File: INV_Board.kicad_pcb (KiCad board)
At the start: 2 copper layers, 100 x 50 mm, 142 parts, among them J1 USB_B_Micro, J10 Conn_01x02_Male, J11 Conn_01x04_Male, J2 Conn_01x02_Male, J3 Conn_01x02_Male, J4 Conn_01x02_Male, J5 Conn_01x04_Male, J6 Conn_01x03_Male, J7 Conn_01x03_Male, J8 Conn_ARM_JTAG_SWD_10, J9 Conn_01x05_Male, Q1 Q_NMOS_GDS, Q2 Q_NMOS_GDS, Q3 Q_NMOS_GDS, Q4 Q_NMOS_GDS, Q5 Q_NMOS_GDS, Q6 Q_NMOS_GDS, U1 LMR36510, U2 STM32F303CBTx, U3 IR2181, U4 IR2181, U5 IR2181, U6 TPS76333, U7 TLV61046ADB, X1 ASE-xxxMHz

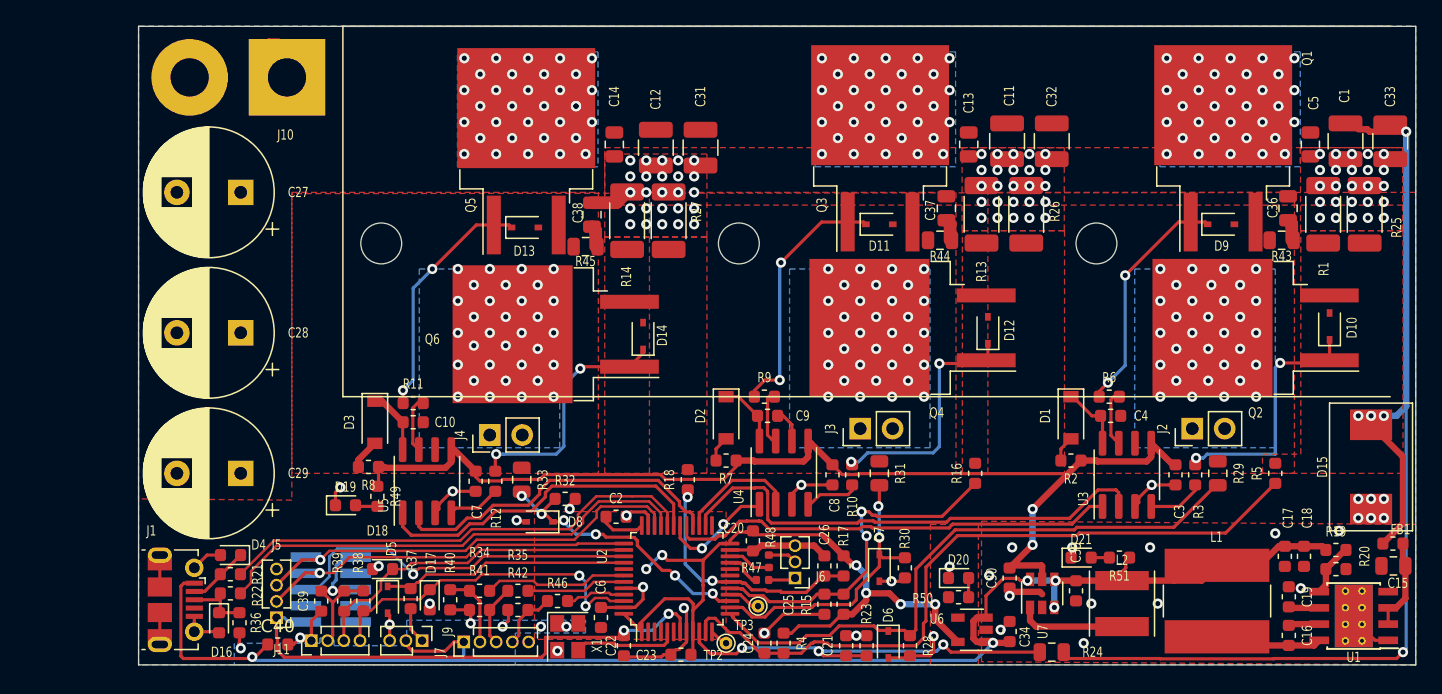
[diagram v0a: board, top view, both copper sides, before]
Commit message: Connectors now JST PH series for throttle and hall sensor input, routing for Iu improved, larger capacitors (2x) 6 pin header to include SWO connectivity, 0402 removed, extra capacitors on Hall sensor lines, extra resistor added to enable use of 100V TI LM5163 chip or LMR36510.
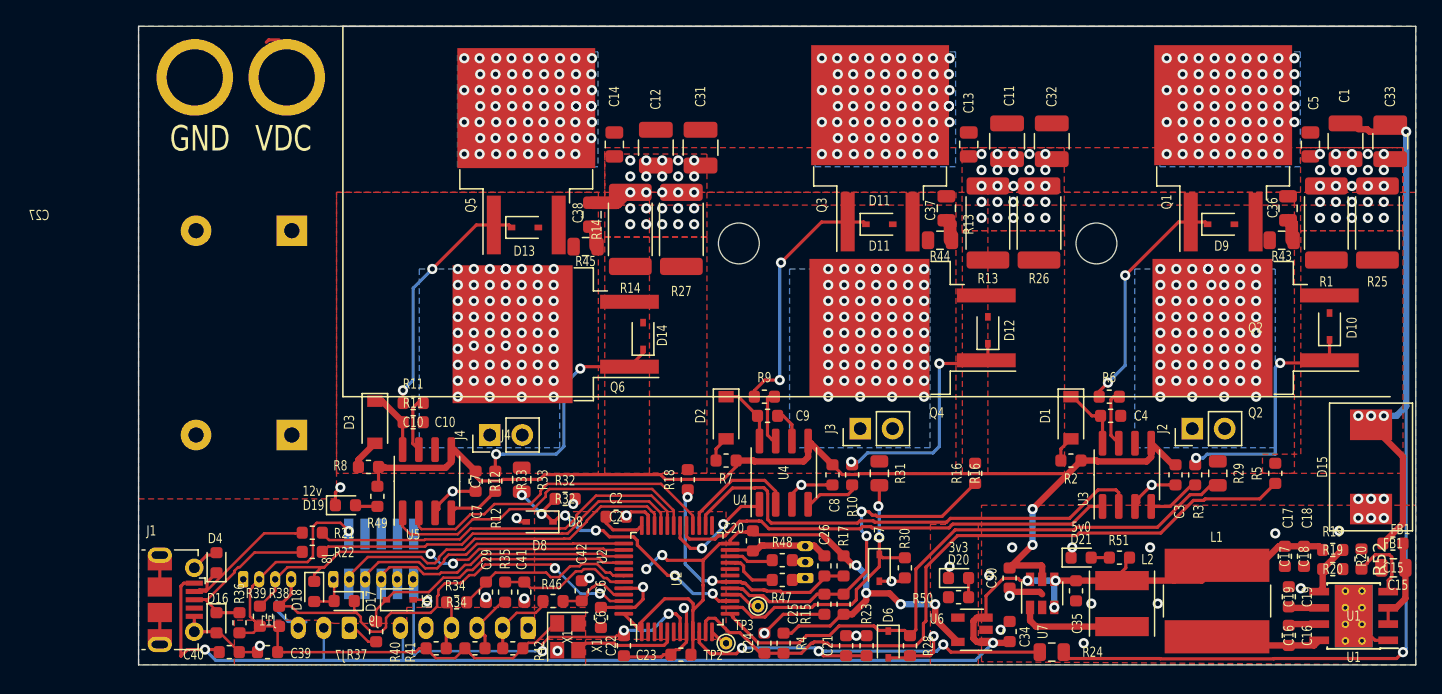
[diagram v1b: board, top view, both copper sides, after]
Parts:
- removed J5: Conn_01x04_Male, Connector_PinHeader_1.27mm:PinHeader_1x04_P1.27mm_Vertical
- added C41: C_100pF_16V, Capacitor_SMD:C_0603_1608Metric, F.Cu at (70.2, 72.3)
- added C42: C_100pF_16V, Capacitor_SMD:C_0603_1608Metric, F.Cu at (74.7, 72.2)
- added J12: Conn_01x06_Female, Connector_JST:JST_PH_B6B-PH-K_1x06_P2.00mm_Vertical, B.Cu at (70.5, 75.1)
- added R52: R_30k, Resistor_SMD:R_0603_1608Metric, F.Cu at (135.8, 69.7)
- C1, C11, C12, C31, C32, C33: value C_10uF 75V -> C_4.7uF 100V
- C21, C24, C25, C26: value C_100pF_25V -> C_100pF_16V
- C27, C28: value CP_220uF -> CP_470uF+; footprint Capacitor_THT:CP_Radial_D10.0mm_P5.00mm -> Capacitor_THT:CP_Radial_D16.0mm_P7.50mm; moved to B.Cu
- C29: value CP_220uF -> C_100pF_16V; footprint Capacitor_THT:CP_Radial_D10.0mm_P5.00mm -> Capacitor_SMD:C_0603_1608Metric
- J10: footprint Connector_Wire:SolderWirePad_1x02_P7.62mm_Drill2.5mm -> INV_Board:XT60; moved to B.Cu
- J11: footprint Connector_PinHeader_1.27mm:PinHeader_1x04_P1.27mm_Vertical -> Connector_Molex:Molex_PicoBlade_53047-0410_1x04_P1.25mm_Vertical; moved to B.Cu
- J6: footprint Connector_PinHeader_1.27mm:PinHeader_1x03_P1.27mm_Vertical -> Connector_Molex:Molex_PicoBlade_53047-0310_1x03_P1.25mm_Vertical; moved to B.Cu
- J7: footprint Connector_PinHeader_1.27mm:PinHeader_1x03_P1.27mm_Vertical -> Connector_JST:JST_PH_B3B-PH-K_1x03_P2.00mm_Vertical; moved to B.Cu
- J9: value Conn_01x05_Male -> Conn_01x06_Male; footprint Connector_PinHeader_1.27mm:PinHeader_1x05_P1.27mm_Vertical -> Connector_Molex:Molex_PicoBlade_53047-0610_1x06_P1.25mm_Vertical; moved to B.Cu
- R1, R13, R14, R25, R26, R27: footprint Resistor_SMD:R_2010_5025Metric -> Resistor_SMD:R_2512_6332Metric
- R47, R48: footprint Resistor_SMD:R_0402_1005Metric -> Resistor_SMD:R_0603_1608Metric
- moved C29 21.3 mm to (67.2, 72.3), turned to 270 degrees
- moved J9 11.3 mm to (55.2, 71.3), turned to 0 degrees
- moved C28 8.94 mm to (52.0, 60.0)
- moved R21 7.19 mm to (53.6, 67.7)
- moved R22 7.19 mm to (53.6, 69.2)
- moved J11 7.17 mm to (48.2, 71.3), turned to 0 degrees
- moved R38 6.71 mm to (51.0, 74.2), turned to 90 degrees
- moved R39 6.71 mm to (49.5, 74.2), turned to 90 degrees
- moved D17 6.70 mm to (56.1, 73.0), turned to 180 degrees
- moved C39 5.80 mm to (50.1, 77.0), turned to 180 degrees
- moved J7 5.79 mm to (56.5, 75.1), turned to 180 degrees
- moved D18 5.63 mm to (53.8, 72.2), turned to 270 degrees
- moved C27 5.00 mm to (52.0, 44.0)
- moved J8 4.62 mm to (59.0, 69.7), turned to 270 degrees
- moved R40 3.96 mm to (63.3, 76.7), turned to 0 degrees
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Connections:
- C29 pad 1: +VDC -> /Hall1
- J9 pad 1: +5V -> GND
- J9 pad 2: Net-(J9-Pad2) -> SWDIO
- J9 pad 3: Net-(J9-Pad3) -> SWCLK
- J9 pad 4: Net-(J9-Pad4) -> SWO
- J9 pad 5: GND -> Net-(J9-Pad5)
- R34 pad 2: Net-(J9-Pad2) -> Net-(J12-Pad4)
- R35 pad 2: Net-(J9-Pad3) -> Net-(J12-Pad3)
- R40 pad 2: Net-(J9-Pad2) -> Net-(J12-Pad4)
- R41 pad 2: Net-(J9-Pad3) -> Net-(J12-Pad3)
- R42 pad 2: Net-(J9-Pad4) -> Net-(J12-Pad2)
- R46 pad 2: Net-(J9-Pad4) -> Net-(J12-Pad2)
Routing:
- net +3V3: track 77.7 -> 103.8 mm, vias 12 -> 7
- net #RES: track 40.3 -> 29.5 mm, vias 2 -> 3
- net I2CSDA: track 26.5 -> 36.0 mm
- net SWO: track 29.6 -> 20.2 mm, vias 1 -> 0
- net /USBDD+: track 38.1 -> 29.6 mm
- net SWCLK: track 30.2 -> 21.8 mm, vias 1 -> 0
- net USBD-: track 4.88 -> 13.2 mm
- net USBD+: track 5.62 -> 13.9 mm
- net /USBDD-: track 37.8 -> 30.4 mm
- net SWDIO: track 34.8 -> 27.8 mm, vias 1 -> 0
- net Net-(J12-Pad2): track 0.00 -> 6.90 mm
- net I2CSCL: track 26.6 -> 33.3 mm, vias 0 -> 2
- net Net-(J9-Pad2): track 6.10 -> 0.00 mm
- net Net-(R52-Pad2): track 0.00 -> 5.77 mm
- net Net-(J9-Pad3): track 5.17 -> 0.00 mm
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- removed copper zone on B.Cu, net +3V3
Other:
- outline, holes or cut-outs redrawn
- board text added: "#Res N/C SWO SWC SWDIO G"
- board text added: "12v"
- board text added: "3v3"
- board text added: "5V H1 H2 H3 N/C G"
- board text added: "5v0"
- board text added: "SDA SCL 3v3 G"
- board text removed: "#Res SWC SWDIO G"
- board text removed: "5V H1 H2 H3 G"
- board text removed: "Cortex 10Pin Header"
- board text removed: "G 3v3 SCL SDA"

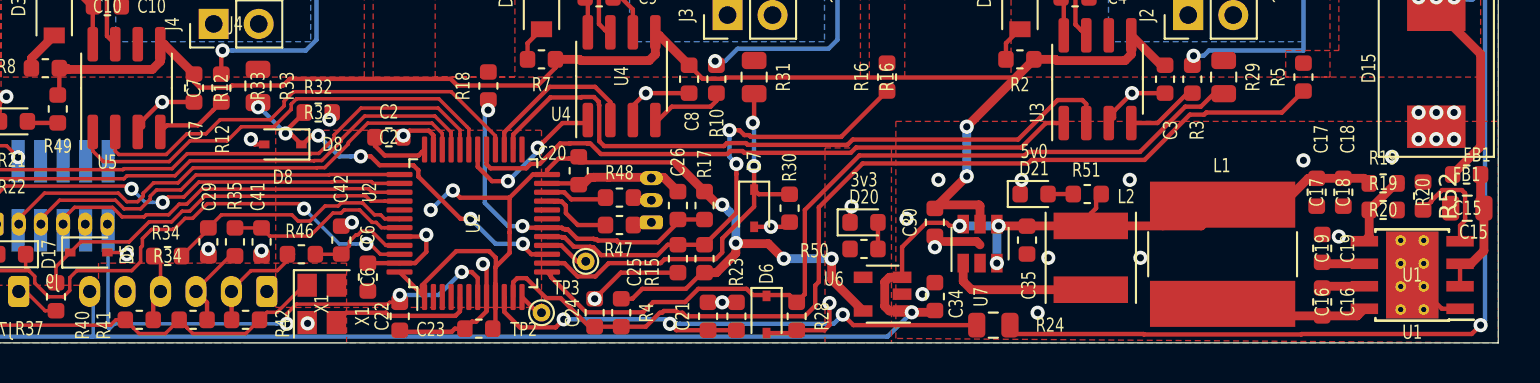
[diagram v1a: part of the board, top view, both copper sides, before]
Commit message: As ordered R2_2. Updated to use TPS61040 since JLCPCB have them as basic parts plus LM5163 capable, for 100V. XT60 PCB mount connectors, large 16mm diameter caps. 5 samples ordered with CRMicro FETs
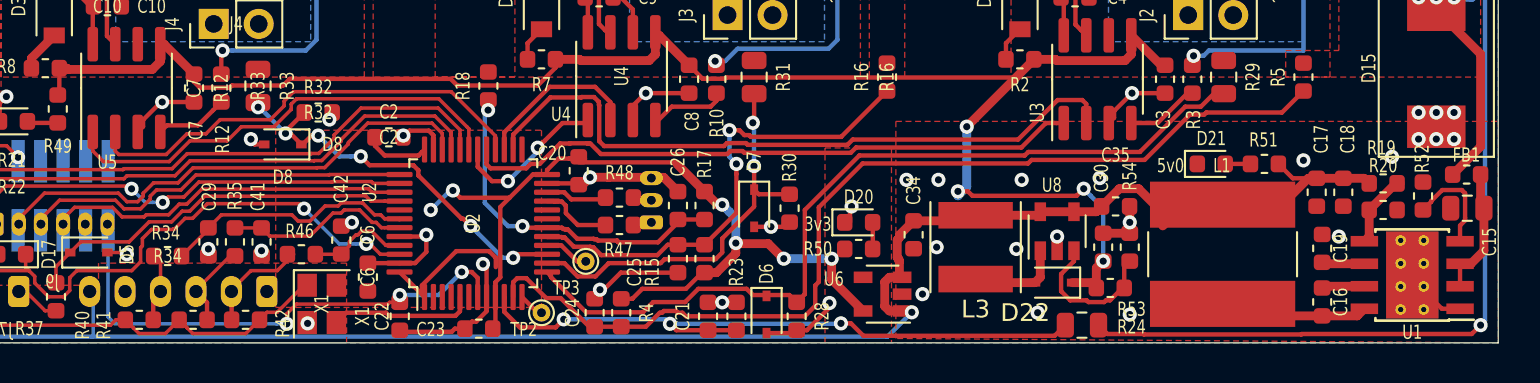
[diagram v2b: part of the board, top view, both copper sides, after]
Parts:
- removed L2: L_15uH_1A, Inductor_SMD:L_Taiyo-Yuden_NR-50xx
- removed U7: TLV61046ADB, Package_TO_SOT_SMD:SOT-23-6
- added D22: BAT48JFILM, Diode_SMD:D_SOD-323, F.Cu at (114.9, 74.6)
- added L3: L_15uH_1A, Inductor_SMD:L_Taiyo-Yuden_NR-50xx, F.Cu at (110.5, 72.6)
- added R53: R_18k, Resistor_SMD:R_0603_1608Metric, F.Cu at (118.1, 74.9)
- added R54: R_4k7, Resistor_SMD:R_0603_1608Metric, F.Cu at (119.2, 72.6)
- added U8: TPS61041DDC, Package_TO_SOT_SMD:SOT-23-5, F.Cu at (115.1, 71.7)
- R24, R29, R31, R33: value R_47k -> R_82k
- moved D21 10.1 mm to (123.8, 67.9)
- moved R51 10.1 mm to (126.8, 67.9)
- moved C30 9.60 mm to (117.7, 72.6), turned to 90 degrees
- moved C35 5.35 mm to (118.4, 70.3), turned to 180 degrees
- moved R24 5.00 mm to (116.5, 77.0)
- moved C34 3.69 mm to (107.0, 71.9), turned to 270 degrees
- moved D20 0.30 mm to (103.9, 71.2)
- moved R50 0.30 mm to (103.9, 72.7)
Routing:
- net +12V: track 87.0 -> 97.0 mm, vias 2 -> 4
- net Net-(L2-Pad2): track 8.42 -> 0.00 mm
- net Net-(R53-Pad1): track 0.00 -> 8.32 mm
- net Net-(D22-Pad2): track 0.00 -> 5.36 mm
- net Vsense_MCU: track 32.6 -> 37.6 mm
- net +VDC: track 89.1 -> 84.1 mm
- net +5V: track 122.4 -> 120.3 mm, vias 5 -> 2
- net GND: track 87.8 -> 89.2 mm, vias 113 -> 116
- net #RES: track 29.5 -> 28.9 mm
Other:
- board text added: "G H3 H2 H1 N/C 5V"
- board text removed: "5V H1 H2 H3 N/C G"

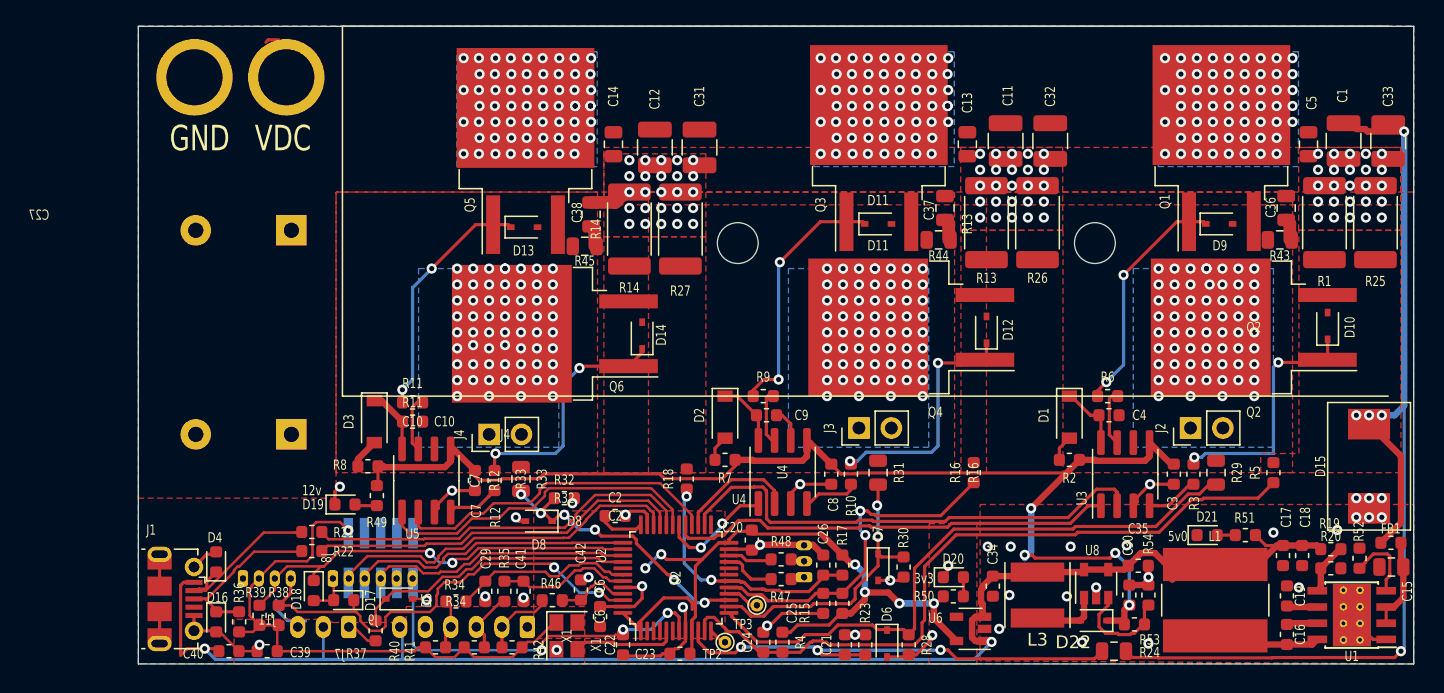
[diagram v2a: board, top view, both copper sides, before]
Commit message: Moved PSU, Added analog in & converted UART to JST PH with VESC pinout, added TP for opamp3, added thermistor, added FAN73901 to the JLCPCB BoM, swapped to LM5017 DCDC, added inductors to BoM, added 20x 1uF 100V ceramic capacitors to BoM, added silkscreen MESC_FOC_ESC.
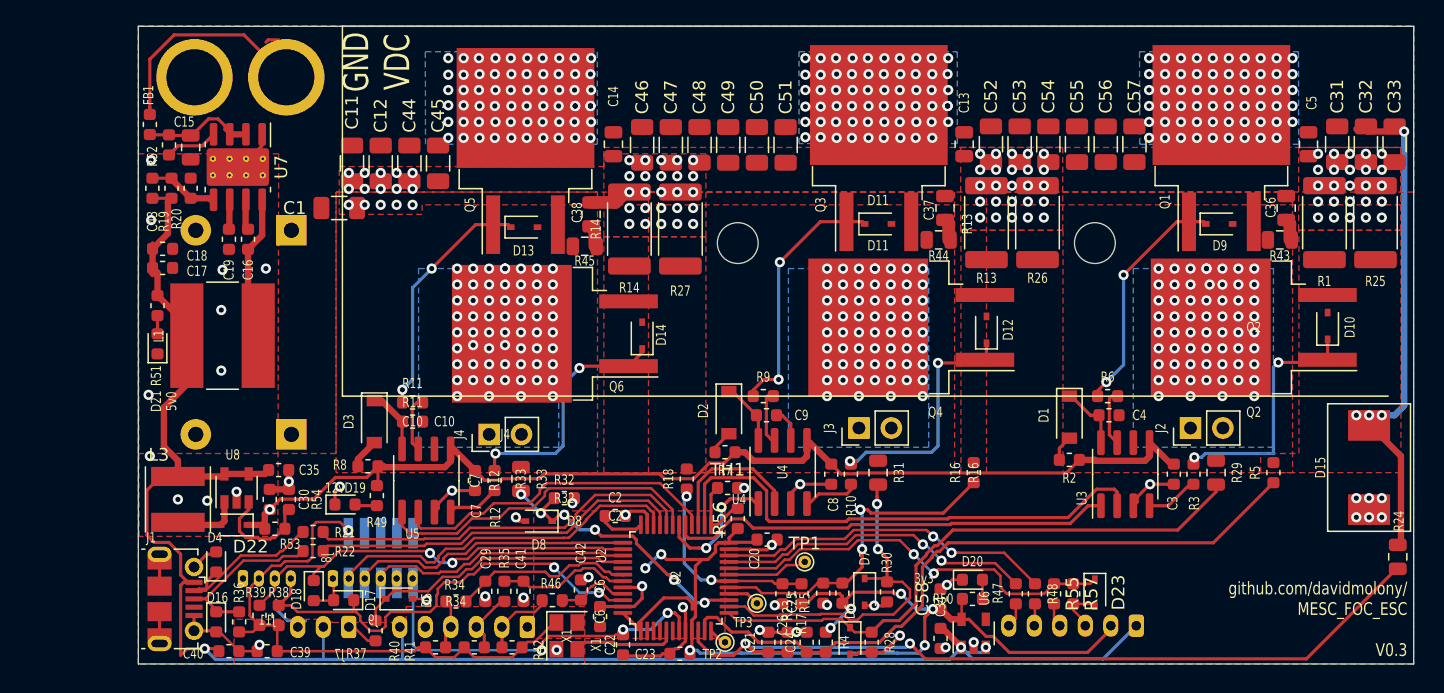
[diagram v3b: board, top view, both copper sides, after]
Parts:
- removed J6: Conn_01x03_Male, Connector_Molex:Molex_PicoBlade_53047-0310_1x03_P1.25mm_Vertical
- removed U1: LMR36510, Package_SO:Texas_HSOP-8-1EP_3.9x4.9mm_P1.27mm_ThermalVias
- added C43: C_100pF_16V, Capacitor_SMD:C_0603_1608Metric, F.Cu at (41.1, 40.7)
- added C44: C_1uF 100V, Capacitor_SMD:C_1206_3216Metric, F.Cu at (61.2, 38.8)
- added C45: C_1uF 100V, Capacitor_SMD:C_1206_3216Metric, F.Cu at (63.5, 38.8)
- added C46: C_1uF 100V, Capacitor_SMD:C_1206_3216Metric, F.Cu at (79.5, 37.3)
- added C47: C_1uF 100V, Capacitor_SMD:C_1206_3216Metric, F.Cu at (81.8, 37.3)
- added C48: C_1uF 100V, Capacitor_SMD:C_1206_3216Metric, F.Cu at (84.0, 37.3)
- added C49: C_1uF 100V, Capacitor_SMD:C_1206_3216Metric, F.Cu at (86.2, 37.3)
- added C50: C_1uF 100V, Capacitor_SMD:C_1206_3216Metric, F.Cu at (88.5, 37.3)
- added C51: C_1uF 100V, Capacitor_SMD:C_1206_3216Metric, F.Cu at (90.8, 37.3)
- added C52: C_1uF 100V, Capacitor_SMD:C_1206_3216Metric, F.Cu at (106.8, 37.2)
- added C53: C_1uF 100V, Capacitor_SMD:C_1206_3216Metric, F.Cu at (109.1, 37.2)
- added C54: C_1uF 100V, Capacitor_SMD:C_1206_3216Metric, F.Cu at (111.3, 37.2)
- added C55: C_1uF 100V, Capacitor_SMD:C_1206_3216Metric, F.Cu at (113.6, 37.2)
- added C56: C_1uF 100V, Capacitor_SMD:C_1206_3216Metric, F.Cu at (115.8, 37.2)
- added C57: C_1uF 100V, Capacitor_SMD:C_1206_3216Metric, F.Cu at (118.1, 37.2)
- added C58: C_10uF_16V, Capacitor_SMD:C_0603_1608Metric, F.Cu at (102.9, 72.9)
- added D23: D_Zener_3v3, Diode_SMD:D_SOD-323, F.Cu at (115.0, 72.4)
- added J5: Conn_01x06_Female, Connector_JST:JST_PH_B6B-PH-K_1x06_P2.00mm_Vertical, B.Cu at (118.2, 75.0)
- added R55: R_1k5, Resistor_SMD:R_0603_1608Metric, F.Cu at (111.8, 72.5)
- added R56: R_4k7, Resistor_SMD:R_0603_1608Metric, F.Cu at (87.0, 66.6)
- added R57: R_1k5, Resistor_SMD:R_0603_1608Metric, F.Cu at (113.3, 72.5)
- added TH1: Thermistor_NTC, Resistor_SMD:R_0603_1608Metric, F.Cu at (86.2, 64.2)
- added TP1: TestPoint, TestPoint:TestPoint_THTPad_D1.0mm_Drill0.5mm, F.Cu at (92.2, 70.0)
- added U7: LM5017MR, Package_SO:SOIC-8-1EP_3.9x4.9mm_P1.27mm_EP2.95x4.9mm_Mask2.71x3.4mm_ThermalVias, F.Cu at (47.8, 39.0)
- C1, C11, C12, C31, C32, C33: value C_4.7uF 100V -> C_1uF 100V; footprint Capacitor_SMD:C_1210_3225Metric -> Capacitor_SMD:C_1206_3216Metric
- C16: value C_1uF_25V -> C_0.1uF_25V
- L1: value L_100uH_1.5A -> L_120uH_1.0A
- L3: value L_15uH_1A -> L_10uH_1A
- R19: value R_18k -> R_15k
- R53: value R_18k -> R_1k5
- R54: value R_4k7 -> R_150
- moved FB1 102.7 mm to (40.9, 35.7), turned to 90 degrees
- moved C15 99.7 mm to (44.1, 37.5), turned to 270 degrees
- moved R52 98.8 mm to (42.4, 37.3), turned to 90 degrees
- moved R19 95.2 mm to (42.6, 40.7), turned to 90 degrees
- moved R20 94.2 mm to (44.1, 40.7), turned to 90 degrees
- moved C18 92.5 mm to (41.9, 45.5), turned to 0 degrees
- moved C17 90.7 mm to (41.9, 47.0), turned to 0 degrees
- moved C19 87.5 mm to (47.1, 44.7), turned to 270 degrees
- moved R51 87.2 mm to (41.5, 49.9), turned to 270 degrees
- moved C16 87.2 mm to (48.6, 44.7), turned to 270 degrees
- moved D21 83.7 mm to (41.5, 52.9), turned to 90 degrees
- moved L1 80.6 mm to (46.6, 52.3), turned to 180 degrees
- moved C1 78.9 mm to (55.8, 42.2), turned to 0 degrees
- moved C30 67.8 mm to (50.3, 65.1)
- moved C35 67.8 mm to (51.0, 62.8)
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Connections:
- net Net-(TP2-Pad1) renamed /op1Vout
- net Net-(TP3-Pad1) renamed /op2Vout
- J10 pad 1: +VDC -> GND
- J10 pad 2: GND -> +VDC
- L1 pad 1: Net-(C16-Pad1) -> Net-(C16-Pad2)
- R52 pad 1: GND -> Net-(R52-Pad1)
- R52 pad 2: Net-(R52-Pad2) -> Net-(C15-Pad1)
- U2 pad 20: Net-(U2-Pad20) -> AnalogIn
- U2 pad 25: Net-(U2-Pad25) -> BoardTemp
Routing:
- net AnalogIn: track 0.00 -> 32.6 mm, vias 0 -> 2
- net +3V3: track 103.8 -> 132.0 mm, vias 7 -> 9
- net Vsense_MCU: track 37.6 -> 64.2 mm, vias 3 -> 2
- net +VDC: track 84.1 -> 59.5 mm, vias 183 -> 185
- net +5V: track 120.3 -> 144.0 mm, vias 2 -> 3
- net STRx: track 3.37 -> 26.4 mm, vias 0 -> 2
- net STTx: track 4.00 -> 24.9 mm, vias 0 -> 2
- net +12V: track 97.0 -> 85.2 mm, vias 4 -> 1
- net Net-(C16-Pad2): track 2.42 -> 11.4 mm
- net /op3Vout: track 0.00 -> 6.35 mm
- net Net-(C16-Pad1): track 8.45 -> 2.28 mm
- net Net-(R52-Pad2): track 5.77 -> 0.00 mm
- net BoardTemp: track 0.00 -> 5.73 mm
- net PhaseV: track 22.8 -> 28.1 mm
- net ISW_MCU: track 20.2 -> 15.8 mm
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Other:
- board text added: "5V 3V3 G An Rx Tx"
- board text added: "I_PhW TP"
- board text added: "github.com/davidmolony/ MESC_FOC_ESC V0.3"
- board text removed: "Tx Rx G"
